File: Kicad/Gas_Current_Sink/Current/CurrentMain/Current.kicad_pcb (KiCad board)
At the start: 2 copper layers, 20 parts, among them J2 ACS770, J3 ACS712, J4 PA3208, J5 SCT, J6 CONN_01X02, P1 PHR-4, U1 LM324N, U2 LM2931AZ-3.3/5.0

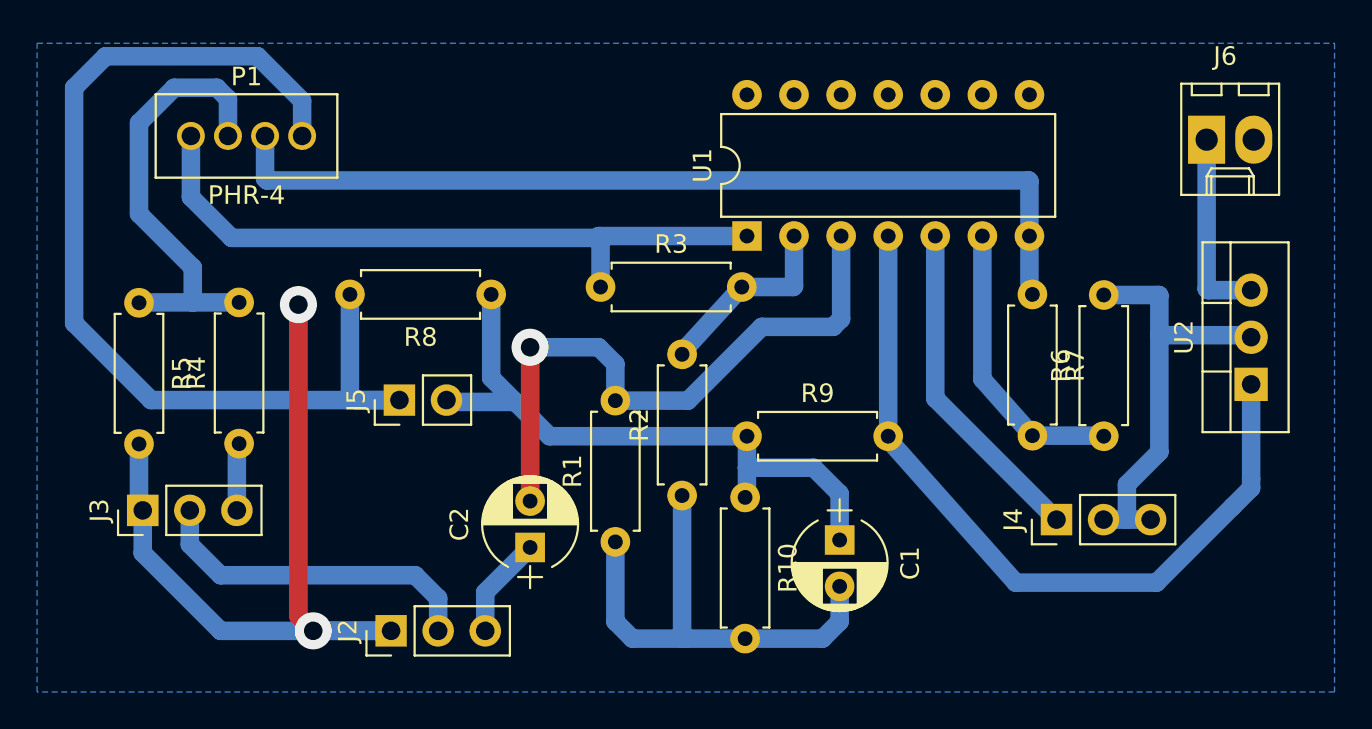
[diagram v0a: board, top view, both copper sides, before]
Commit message: Minor changes on pcb routing.
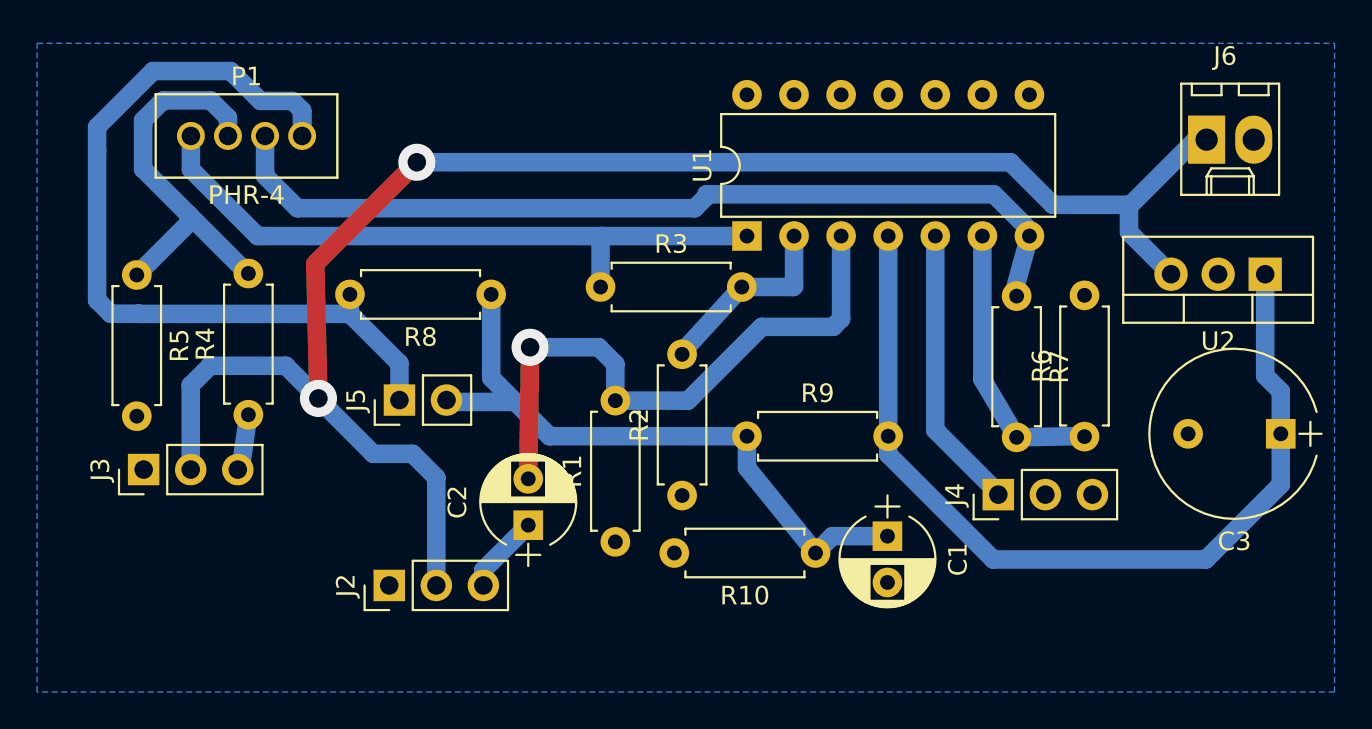
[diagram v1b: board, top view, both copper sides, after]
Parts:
- added C3: 10u1, Capacitors_THT:CP_Radial_Tantal_D9.0mm_P5.00mm, F.Cu at (188.1, 106.1)
- moved U2 5.99 mm to (187.3, 97.5), turned to 180 degrees
- moved R10 4.84 mm to (163.0, 112.5), turned to 180 degrees
- moved J4 3.42 mm to (172.9, 109.3)
- moved C1 2.59 mm to (166.9, 111.6)
- moved J2 2.45 mm to (140.0, 114.2)
- moved J3 2.20 mm to (126.8, 108.0)
- moved R4 1.64 mm to (132.4, 105.0)
- moved R5 1.50 mm to (126.4, 97.5)
- moved C2 1.20 mm to (147.5, 111.0)
- moved R6 1.04 mm to (177.5, 106.2)
- moved R7 0.85 mm to (173.8, 98.6)
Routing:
- net GND: track 95.9 -> 0.06 mm, vias 2 -> 0
- net +5V: track 36.9 -> 91.5 mm, vias 0 -> 2
- net Net-(J5-Pad1): track 56.0 -> 46.0 mm
- net +3V3: track 41.8 -> 48.9 mm
- net Net-(J4-Pad1): track 18.0 -> 15.4 mm
- net Net-(P1-Pad2): track 24.4 -> 21.8 mm
- net Net-(C2-Pad1): track 5.50 -> 4.25 mm
- net Net-(C2-Pad2): track 34.0 -> 32.8 mm
- net Net-(R6-Pad1): track 19.8 -> 18.7 mm
- net Net-(P1-Pad1): track 37.3 -> 36.3 mm
- net Net-(P1-Pad3): track 50.0 -> 49.3 mm
- net Net-(C1-Pad1): track 35.0 -> 35.7 mm

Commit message: Added some lables to schematic.
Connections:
- net Net-(J5-Pad1) renamed /SCT
- net Net-(P1-Pad1) renamed /ACS770
- net Net-(P1-Pad2) renamed /ACS712
- net Net-(P1-Pad3) renamed /PA3208
